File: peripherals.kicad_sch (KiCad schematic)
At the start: 74 parts, among them J10 533980471, J11 ERF8-040-05.0-L-DV-K-TR, J9 TC2050-IDC-NL, Q10 NX138BKMYL, Q9 NX138BKMYL, U29 TPD4E05U06QDQARQ1, U30 TPD4E05U06QDQARQ1, U33 NTS0102GT, U34 PCAL6408ABSHP

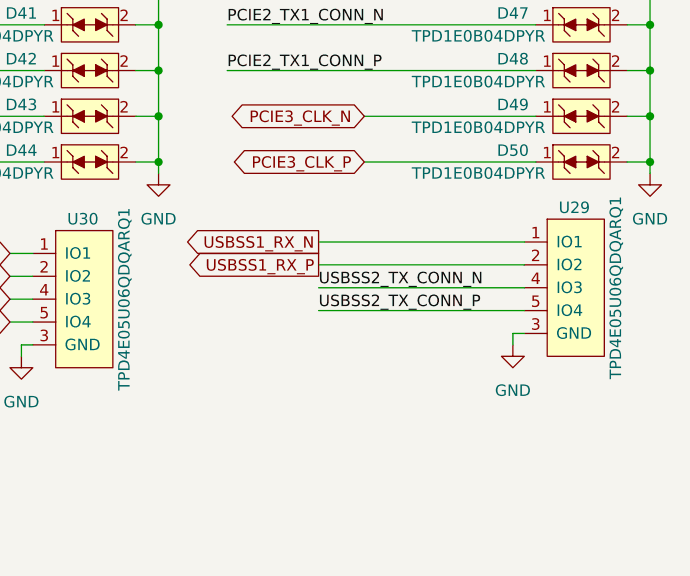
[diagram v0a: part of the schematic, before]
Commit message: Routed USB SS to exp connector, improved high speed routing
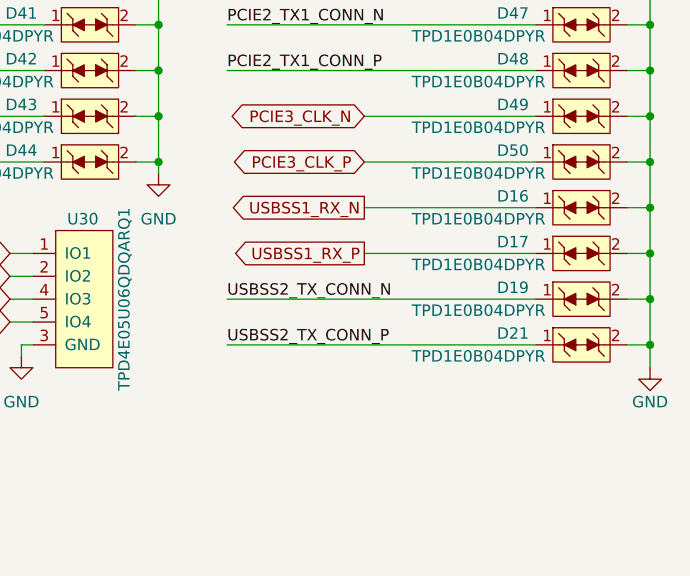
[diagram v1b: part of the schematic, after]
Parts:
- removed U29: TPD4E05U06QDQARQ1, antmicro-footprints:USON-10_2.5x1.0mm_P0.5mm, symbol antmicroTVSDiodes:TPD4E05U06QDQARQ1
- added D16, D17, D19, D21: TPD1E0B04DPYR, antmicro-footprints:XDFN-2_1x0.60mm, symbol antmicroTVSDiodes:TPD1E0B04DPYR
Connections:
- net GND: now also D16.2, D17.2, D19.2, D21.2
- net USBSS1_RX_N: now also D16.1
- net USBSS1_RX_P: now also D17.1
- net USBSS2_TX_CONN_N: now also D19.1
- net USBSS2_TX_CONN_P: now also D21.1

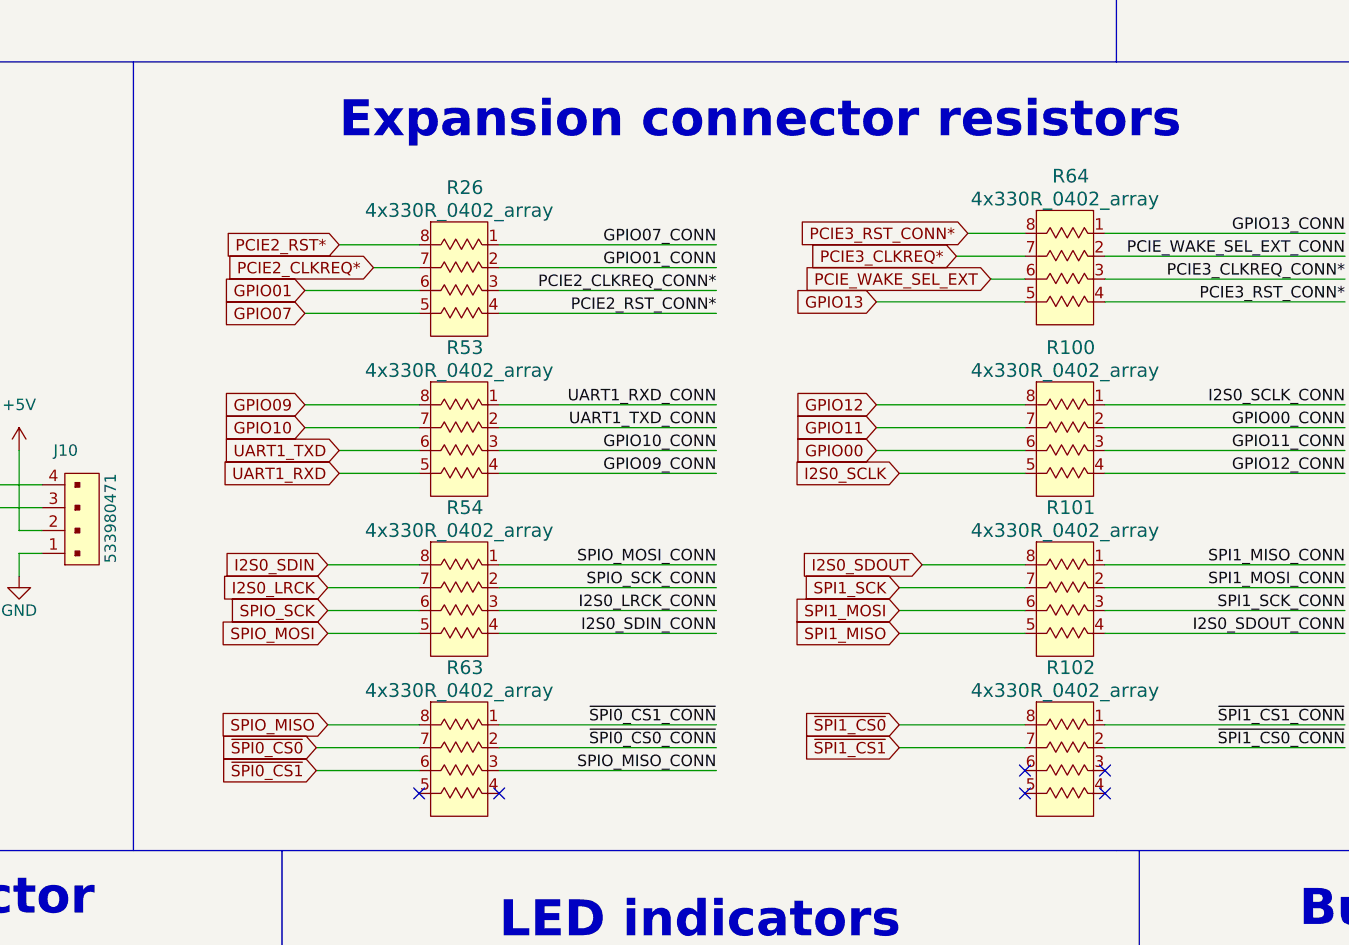
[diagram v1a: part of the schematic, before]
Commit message: Added exp conn resistors
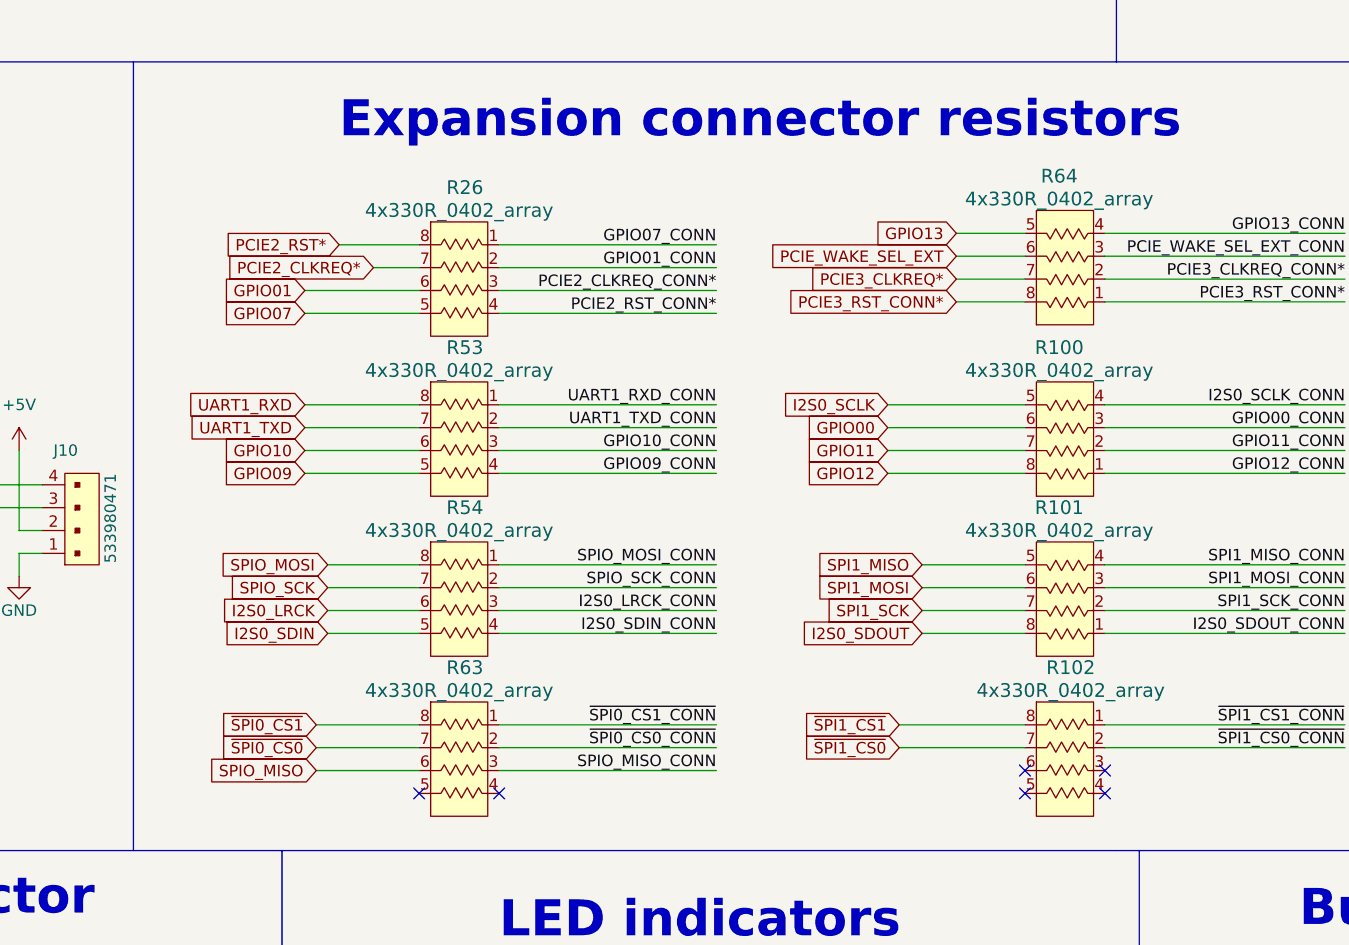
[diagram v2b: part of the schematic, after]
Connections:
- net GPIO00_CONN: now also R100.3; no longer R100.2
- net GPIO09: now also R53.5; no longer R53.8
- net GPIO10: now also R53.6; no longer R53.7
- net GPIO11_CONN: now also R100.2; no longer R100.3
- net GPIO12_CONN: now also R100.1; no longer R100.4
- net GPIO13_CONN: now also R64.4; no longer R64.1
- net I2S0_LRCK: now also R54.6; no longer R54.7
- net I2S0_SCLK_CONN: now also R100.4; no longer R100.1
- net I2S0_SDIN: now also R54.5; no longer R54.8
- net I2S0_SDOUT_CONN: now also R101.1; no longer R101.4
- net PCIE3_CLKREQ_CONN*: now also R64.2; no longer R64.3
- net PCIE3_RST_CONN*: now also R64.1; no longer R64.4
- net PCIE_WAKE_SEL_EXT_CONN: now also R64.3; no longer R64.2
- net SPI1_MISO_CONN: now also R101.4; no longer R101.1
- net SPI1_MOSI_CONN: now also R101.3; no longer R101.2
- net SPI1_SCK_CONN: now also R101.2; no longer R101.3
- net SPIO_MISO: now also R63.6; no longer R63.8
- net SPIO_MOSI: now also R54.8; no longer R54.5
- net SPIO_SCK: now also R54.7; no longer R54.6
- net UART1_RXD: now also R53.8; no longer R53.5
- net UART1_TXD: now also R53.7; no longer R53.6
- net ~{SPI0_CS1}: now also R63.8; no longer R63.6
- net ~{SPI1_CS0}: now also R102.7; no longer R102.8
- net ~{SPI1_CS1}: now also R102.8; no longer R102.7
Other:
- moved on the sheet: R100, R101, R64

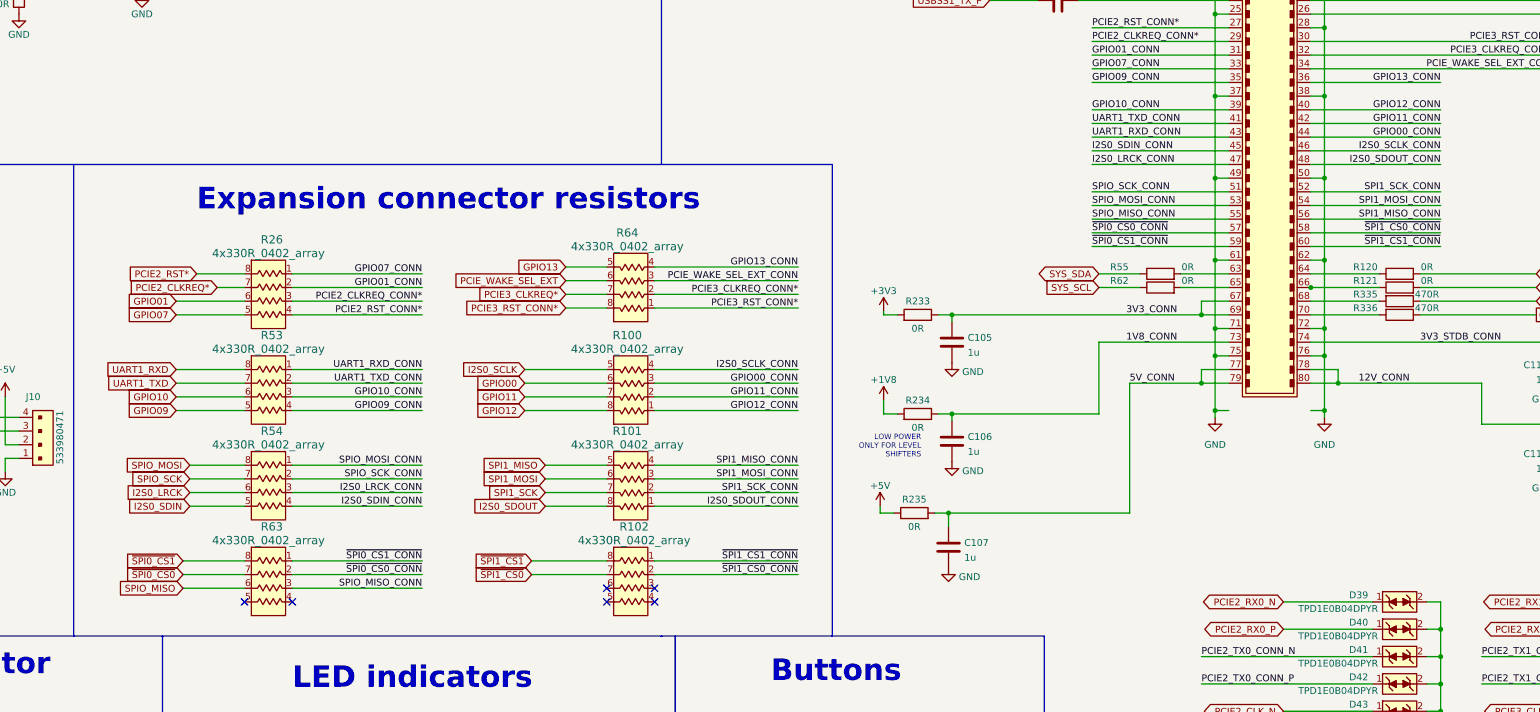
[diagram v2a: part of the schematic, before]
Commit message: Routed most low speed signals to exp connector
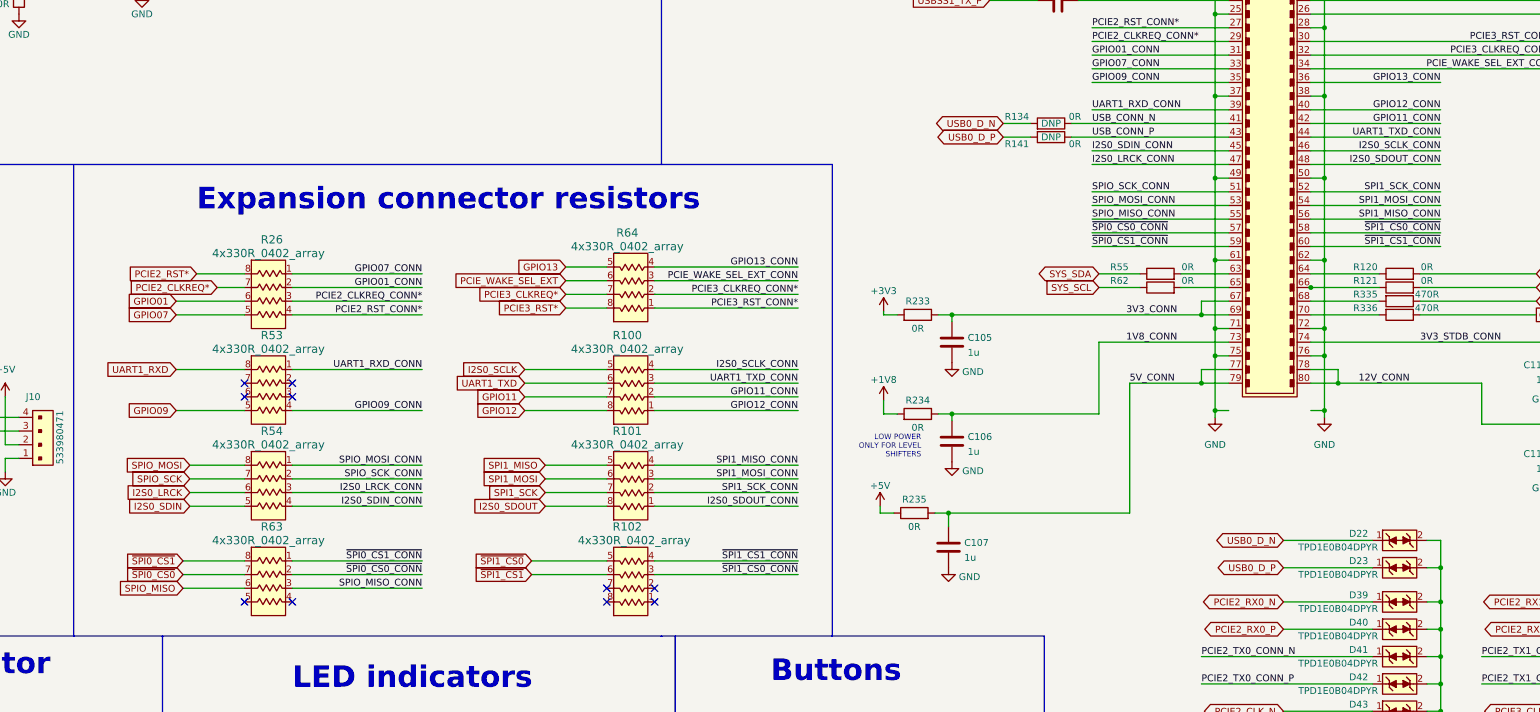
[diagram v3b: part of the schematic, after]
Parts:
- added D22, D23: TPD1E0B04DPYR, antmicro-footprints:XDFN-2_1x0.60mm, symbol antmicroTVSDiodes:TPD1E0B04DPYR
- added R134, R141: R_0R_0402, antmicro-footprints:0402-res, symbol antmicroResistors0402:R_0R_0402
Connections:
- net GPIO00 is gone; now on net UART1_TXD: R100.6
- net GPIO00_CONN is gone; now on net UART1_TXD_CONN: J11.44, R100.3
- net GND: now also D22.2, D23.2
- net PCIE3_RST_CONN*: no longer R64.8
- net UART1_RXD_CONN: now also J11.39; no longer J11.43
- net UART1_TXD: no longer R53.7
- net UART1_TXD_CONN: no longer J11.41, R53.2
- net ~{SPI1_CS0_CONN}: now also R102.3; no longer R102.2
- net ~{SPI1_CS0}: now also R102.5; no longer R102.7
- net ~{SPI1_CS1_CONN}: now also R102.4; no longer R102.1
- net ~{SPI1_CS1}: now also R102.6; no longer R102.8
- net GPIO10: no longer names the net of R53.6
- net GPIO10_CONN: no longer names the net of R53.3
- net GPIO10_CONN: no longer J11.39
- new net PCIE3_RST*: R64.8
- new net USB0_D_N: D22.1, R134.2
- new net USB0_D_P: D23.1, R141.2
- new net USB_CONN_N: J11.41, R134.1
- new net USB_CONN_P: J11.43, R141.1
- no-connect marks 6 -> 10
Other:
- moved on the sheet: R102

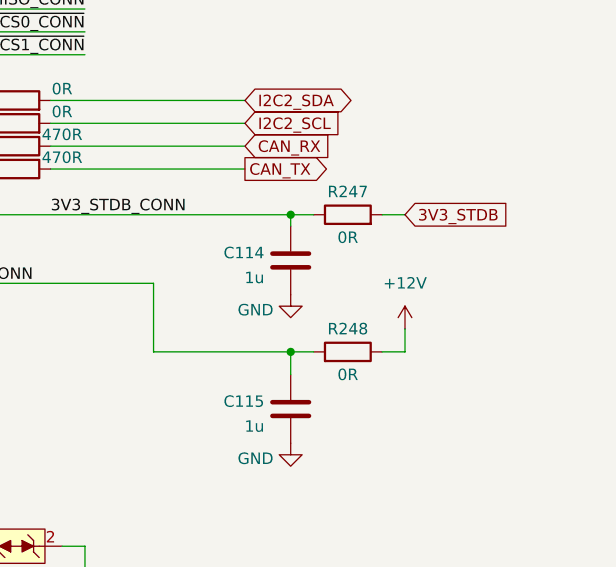
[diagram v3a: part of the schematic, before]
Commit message: Routed more low speed signal and power
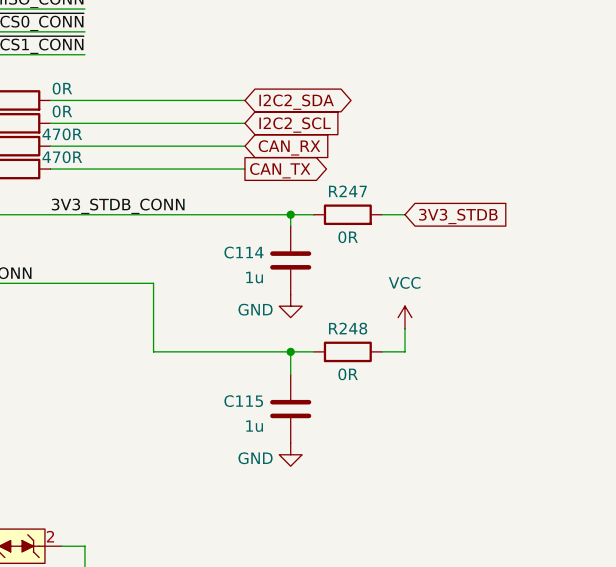
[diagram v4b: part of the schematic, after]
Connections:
- net +12V renamed VCC
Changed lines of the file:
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@@
     (pin "8")
-  )
-  (symbol (lib_id "power:+12V") (at 379.73 163.83 0) (unit 1)
-    (in_bom yes) (on_board yes) (fields_autoplaced)
-    (property "Reference" "#PWR0248" (id 0) (at 379.73 167.64 0)
-      (effects (font (size 1.27 1.27)) hide)
-    )
-    (property "Value" "+12V" (id 1) (at 379.73 158.75 0))
-    (property "Footprint" "" (id 2) (at 379.73 163.83 0)
-      (effects (font (size 1.27 1.27)) hide)
-    )
-    (property "Datasheet" "" (id 3) (at 379.73 163.83 0)
-      (effects (font (size 1.27 1.27)) hide)
-    )
-    (pin "1")
   )
   (symbol (lib_id "antmicroResistors0402:R_100k_0402") (at 127 260.35 90) (unit 1)
@@
       (effects (font (size 1.27 1.27)) hide)
     )
+    (pin "1")
+  )
+  (symbol (lib_id "power:VCC") (at 379.73 163.83 0) (unit 1)
+    (in_bom yes) (on_board yes) (fields_autoplaced)
+    (property "Reference" "#PWR0175" (id 0) (at 379.73 167.64 0)
+      (effects (font (size 1.27 1.27)) hide)
+    )
+    (property "Value" "VCC" (id 1) (at 379.73 158.75 0))
+    (property "Footprint" "" (id 2) (at 379.73 163.83 0)
+      (effects (font (size 1.27 1.27)) hide)
+    )
+    (property "Datasheet" "" (id 3) (at 379.73 163.83 0)
+      (effects (font (size 1.27 1.27)) hide)
+    )
